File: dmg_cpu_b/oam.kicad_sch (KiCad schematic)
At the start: 130 parts

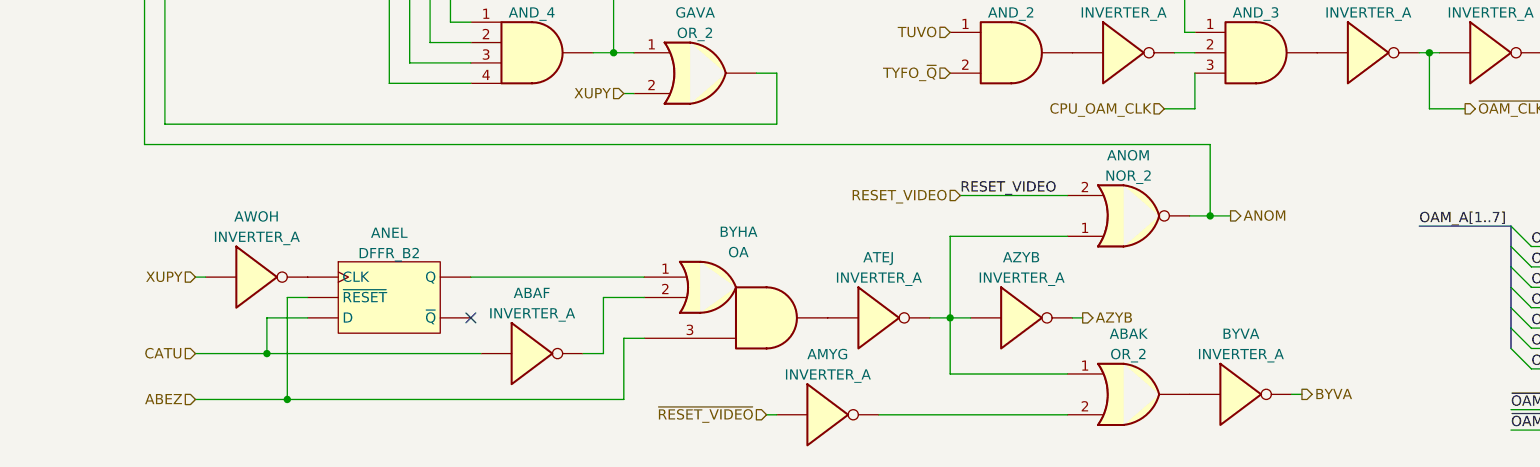
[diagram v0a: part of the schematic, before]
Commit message: sprite y comparator added
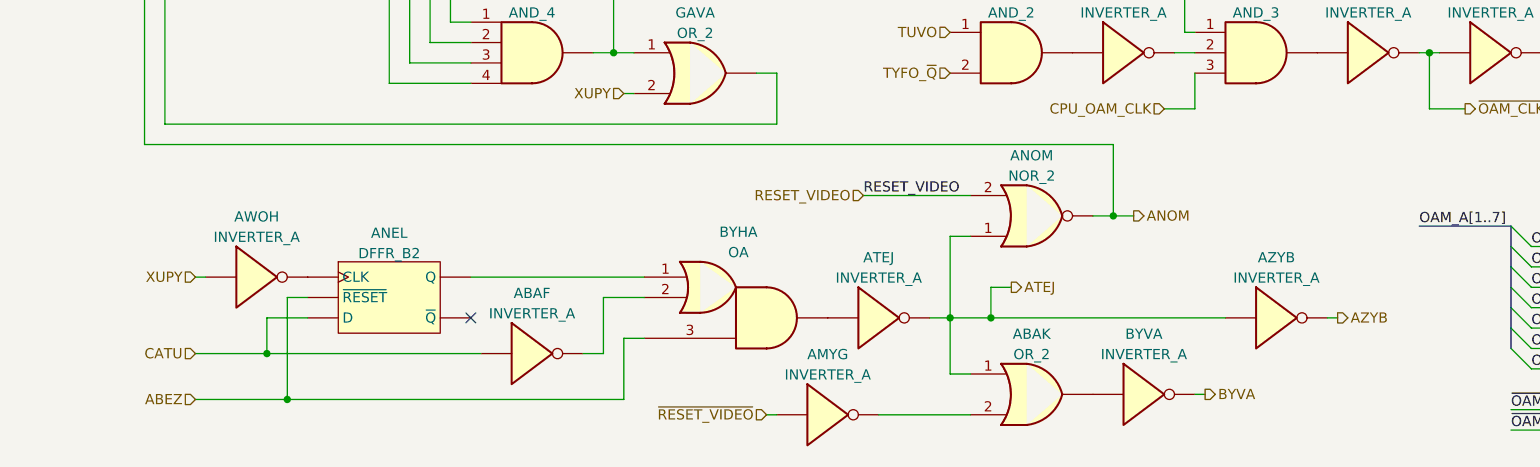
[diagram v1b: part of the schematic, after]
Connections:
- net ATEJ: now reaches ABAK.1, ANOM.1, ATEJ.2, AZYB.1
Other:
- moved on the sheet: ABAK, ANOM, AZYB, BYVA
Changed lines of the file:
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@@
   (junction (at 50.8 196.85) (diameter 0) (color 0 0 0 0)
   )
+  (junction (at 120.65 267.97) (diameter 0) (color 0 0 0 0)
+  )
   (junction (at 15.24 179.705) (diameter 0) (color 0 0 0 0)
   )
@@
   (junction (at 70.485 24.13) (diameter 0) (color 0 0 0 0)
   )
-  (junction (at 147.955 255.27) (diameter 0) (color 0 0 0 0)
+  (junction (at 135.89 255.27) (diameter 0) (color 0 0 0 0)
   )
   (junction (at 197.485 50.8) (diameter 0) (color 0 0 0 0)
@@
     (stroke (width 0) (type default) (color 0 0 0 0))
   )
-  (wire (pts (xy 115.57 267.97) (xy 118.11 267.97))
+  (wire (pts (xy 115.57 267.97) (xy 120.65 267.97))
     (stroke (width 0) (type default) (color 0 0 0 0))
   )
@@
     (stroke (width 0) (type default) (color 0 0 0 0))
   )
-  (wire (pts (xy 130.81 267.97) (xy 132.08 267.97))
+  (wire (pts (xy 162.56 267.97) (xy 163.83 267.97))
     (stroke (width 0) (type default) (color 0 0 0 0))
   )
@@
     (stroke (width 0) (type default) (color 0 0 0 0))
   )
+  (wire (pts (xy 120.65 267.97) (xy 149.86 267.97))
+    (stroke (width 0) (type default) (color 0 0 0 0))
+  )
   (wire (pts (xy 241.935 171.45) (xy 241.935 186.055))
     (stroke (width 0) (type default) (color 0 0 0 0))
@@
     (stroke (width 0) (type default) (color 0 0 0 0))
   )
-  (wire (pts (xy 130.175 280.035) (xy 106.68 280.035))
+  (wire (pts (xy 118.11 280.035) (xy 106.68 280.035))
     (stroke (width 0) (type default) (color 0 0 0 0))
   )
@@
     (stroke (width 0) (type default) (color 0 0 0 0))
   )
-  (wire (pts (xy 116.84 252.73) (xy 130.175 252.73))
+  (wire (pts (xy 104.775 252.73) (xy 118.11 252.73))
     (stroke (width 0) (type default) (color 0 0 0 0))
   )
@@
     (stroke (width 0) (type default) (color 0 0 0 0))
   )
+  (wire (pts (xy 123.19 264.16) (xy 120.65 264.16))
+    (stroke (width 0) (type default) (color 0 0 0 0))
+  )
   (wire (pts (xy 373.38 156.845) (xy 373.38 171.45))
     (stroke (width 0) (type default) (color 0 0 0 0))
@@
     (stroke (width 0) (type default) (color 0 0 0 0))
   )
-  (wire (pts (xy 147.955 255.27) (xy 145.415 255.27))
+  (wire (pts (xy 135.89 255.27) (xy 133.35 255.27))
     (stroke (width 0) (type default) (color 0 0 0 0))
   )
@@
     (stroke (width 0) (type default) (color 0 0 0 0))
   )
-  (wire (pts (xy 158.115 277.495) (xy 159.385 277.495))
+  (wire (pts (xy 146.05 277.495) (xy 147.32 277.495))
     (stroke (width 0) (type default) (color 0 0 0 0))
   )
@@
     (stroke (width 0) (type default) (color 0 0 0 0))
   )
-  (wire (pts (xy 115.57 274.955) (xy 130.175 274.955))
+  (wire (pts (xy 115.57 274.955) (xy 118.11 274.955))
     (stroke (width 0) (type default) (color 0 0 0 0))
   )
@@
     (stroke (width 0) (type default) (color 0 0 0 0))
   )
-  (wire (pts (xy 147.955 246.38) (xy 147.955 255.27))
+  (wire (pts (xy 135.89 246.38) (xy 135.89 255.27))
     (stroke (width 0) (type default) (color 0 0 0 0))
   )
@@
     (stroke (width 0) (type default) (color 0 0 0 0))
   )
+  (wire (pts (xy 120.65 264.16) (xy 120.65 267.97))
+    (stroke (width 0) (type default) (color 0 0 0 0))
+  )
   (wire (pts (xy 344.805 133.985) (xy 358.14 133.985))
     (stroke (width 0) (type default) (color 0 0 0 0))
@@
     (stroke (width 0) (type default) (color 0 0 0 0))
   )
-  (wire (pts (xy 15.24 246.38) (xy 147.955 246.38))
+  (wire (pts (xy 15.24 246.38) (xy 135.89 246.38))
     (stroke (width 0) (type default) (color 0 0 0 0))
   )
@@
     (stroke (width 0) (type default) (color 0 0 0 0))
   )
-  (wire (pts (xy 150.495 255.27) (xy 147.955 255.27))
+  (wire (pts (xy 138.43 255.27) (xy 135.89 255.27))
     (stroke (width 0) (type default) (color 0 0 0 0))
   )
@@
     (stroke (width 0) (type default) (color 0 0 0 0))
   )
-  (wire (pts (xy 130.175 257.81) (xy 115.57 257.81))
+  (wire (pts (xy 118.11 257.81) (xy 115.57 257.81))
     (stroke (width 0) (type default) (color 0 0 0 0))
   )
@@
     (effects (font (size 1.27 1.27)) (justify right bottom))
   )
-  (label "RESET_VIDEO" (at 116.84 252.73 0)
+  (label "RESET_VIDEO" (at 104.775 252.73 0)
     (effects (font (size 1.27 1.27)) (justify left bottom))
   )
@@
     (effects (font (size 1.27 1.27)) (justify left))
   )
-  (hierarchical_label "BYVA" (shape output) (at 159.385 277.495 0)
+  (hierarchical_label "BYVA" (shape output) (at 147.32 277.495 0)
     (effects (font (size 1.27 1.27)) (justify left))
   )
@@
     (effects (font (size 1.27 1.27)) (justify right))
   )
+  (hierarchical_label "ATEJ" (shape output) (at 123.19 264.16 0)
+    (effects (font (size 1.27 1.27)) (justify left))
+  )
   (hierarchical_label "AVAP" (shape input) (at 86.36 209.55 180)
     (effects (font (size 1.27 1.27)) (justify right))
   )
-  (hierarchical_label "AZYB" (shape output) (at 132.08 267.97 0)
+  (hierarchical_label "AZYB" (shape output) (at 163.83 267.97 0)
     (effects (font (size 1.27 1.27)) (justify left))
   )
@@
     (effects (font (size 1.27 1.27)) (justify right))
   )
-  (hierarchical_label "ANOM" (shape output) (at 150.495 255.27 0)
+  (hierarchical_label "ANOM" (shape output) (at 138.43 255.27 0)
     (effects (font (size 1.27 1.27)) (justify left))
   )
@@
     (effects (font (size 1.27 1.27)) (justify right))
   )
-  (hierarchical_label "RESET_VIDEO" (shape input) (at 116.84 252.73 180)
+  (hierarchical_label "RESET_VIDEO" (shape input) (at 104.775 252.73 180)
     (effects (font (size 1.27 1.27)) (justify right))
   )
@@
     (pin "2")
   )
-  (symbol (lib_id "DMG_CPU_Cells:INVERTER_A") (at 151.765 277.495 0) (unit 1)
+  (symbol (lib_id "DMG_CPU_Cells:INVERTER_A") (at 139.7 277.495 0) (unit 1)
     (in_bom yes) (on_board yes) (fields_autoplaced)
-    (property "Reference" "BYVA" (id 0) (at 151.765 269.9852 0))
-    (property "Value" "INVERTER_A" (id 1) (at 151.765 272.5221 0))
-    (property "Footprint" "" (id 2) (at 149.225 277.495 0)
+    (property "Reference" "BYVA" (id 0) (at 139.7 269.9852 0))
+    (property "Value" "INVERTER_A" (id 1) (at 139.7 272.5221 0))
+    (property "Footprint" "" (id 2) (at 137.16 277.495 0)
       (effects (font (size 1.27 1.27)) hide)
     )
-    (property "Datasheet" "http://iceboy.a-singer.de/doc/dmg_cells.html#inv_a" (id 3) (at 153.035 285.115 0)
+    (property "Datasheet" "http://iceboy.a-singer.de/doc/dmg_cells.html#inv_a" (id 3) (at 140.97 285.115 0)
       (effects (font (size 1.27 1.27)) hide)
     )
@@
     (pin "2")
   )
-  (symbol (lib_id "DMG_CPU_Cells:OR_2") (at 137.795 277.495 0) (unit 1)
+  (symbol (lib_id "DMG_CPU_Cells:OR_2") (at 125.73 277.495 0) (unit 1)
     (in_bom yes) (on_board yes) (fields_autoplaced)
-    (property "Reference" "ABAK" (id 0) (at 137.7948 269.9852 0))
-    (property "Value" "OR_2" (id 1) (at 137.7948 272.5221 0))
-    (property "Footprint" "" (id 2) (at 137.541 277.495 0)
+    (property "Reference" "ABAK" (id 0) (at 125.7298 269.9852 0))
+    (property "Value" "OR_2" (id 1) (at 125.7298 272.5221 0))
+    (property "Footprint" "" (id 2) (at 125.476 277.495 0)
       (effects (font (size 1.27 1.27)) hide)
     )
-    (property "Datasheet" "http://iceboy.a-singer.de/doc/dmg_cells.html#or2" (id 3) (at 137.795 285.115 0)
+    (property "Datasheet" "http://iceboy.a-singer.de/doc/dmg_cells.html#or2" (id 3) (at 125.73 285.115 0)
       (effects (font (size 1.27 1.27)) hide)
     )
@@
     (pin "1")
   )
-  (symbol (lib_id "DMG_CPU_Cells:NOR_2") (at 137.795 255.27 0) (mirror x) (unit 1)
+  (symbol (lib_id "DMG_CPU_Cells:NOR_2") (at 125.73 255.27 0) (mirror x) (unit 1)
     (in_bom yes) (on_board yes) (fields_autoplaced)
-    (property "Reference" "ANOM" (id 0) (at 137.7948 247.7602 0))
-    (property "Value" "NOR_2" (id 1) (at 137.7948 250.2971 0))
-    (property "Footprint" "" (id 2) (at 137.541 255.27 0)
+    (property "Reference" "ANOM" (id 0) (at 125.7298 247.7602 0))
+    (property "Value" "NOR_2" (id 1) (at 125.7298 250.2971 0))
+    (property "Footprint" "" (id 2) (at 125.476 255.27 0)
       (effects (font (size 1.27 1.27)) hide)
     )
-    (property "Datasheet" "http://iceboy.a-singer.de/doc/dmg_cells.html#nor2" (id 3) (at 137.795 247.65 0)
+    (property "Datasheet" "http://iceboy.a-singer.de/doc/dmg_cells.html#nor2" (id 3) (at 125.73 247.65 0)
       (effects (font (size 1.27 1.27)) hide)
     )
@@
     (pin "3")
   )
-  (symbol (lib_id "DMG_CPU_Cells:INVERTER_A") (at 124.46 267.97 0) (unit 1)
+  (symbol (lib_id "DMG_CPU_Cells:INVERTER_A") (at 156.21 267.97 0) (unit 1)
     (in_bom yes) (on_board yes) (fields_autoplaced)
-    (property "Reference" "AZYB" (id 0) (at 124.46 260.4602 0))
-    (property "Value" "INVERTER_A" (id 1) (at 124.46 262.9971 0))
-    (property "Footprint" "" (id 2) (at 121.92 267.97 0)
+    (property "Reference" "AZYB" (id 0) (at 156.21 260.4602 0))
+    (property "Value" "INVERTER_A" (id 1) (at 156.21 262.9971 0))
+    (property "Footprint" "" (id 2) (at 153.67 267.97 0)
       (effects (font (size 1.27 1.27)) hide)
     )
-    (property "Datasheet" "http://iceboy.a-singer.de/doc/dmg_cells.html#inv_a" (id 3) (at 125.73 275.59 0)
+    (property "Datasheet" "http://iceboy.a-singer.de/doc/dmg_cells.html#inv_a" (id 3) (at 157.48 275.59 0)
       (effects (font (size 1.27 1.27)) hide)
     )

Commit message: more oam sheets added. Some are still work in progress.
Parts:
- removed ABAF, AMYG, ATEJ, AWOH, AZYB, BYVA, XUJA: INVERTER_A, symbol DMG_CPU_Cells:INVERTER_A
- removed ABAK, ASEN, GAVA: OR_2, symbol DMG_CPU_Cells:OR_2
- removed ANEL, ELYN, FAHA, FONY, GOSO, WEWY, YFEL: DFFR_B2, symbol DMG_CPU_Cells:DFFR_B2
- removed ANOM: NOR_2, symbol DMG_CPU_Cells:NOR_2
- removed BESU: NOR_LATCH, symbol DMG_CPU_Cells:NOR_LATCH
- removed BYHA: OA, symbol DMG_CPU_Cells:OA
- removed FETO: AND_4, symbol DMG_CPU_Cells:AND_4
- removed WEFY: AND_2, symbol DMG_CPU_Cells:AND_2
- added CYKE, WUDA: INVERTER_B, symbol DMG_CPU_Cells:INVERTER_B
- added WEZA, WUCO, WUZY, WYDA, WYSE, ZYSU: TRI_INV_IF0, symbol DMG_CPU_Cells:TRI_INV_IF0
- added XADU, XECU, XEDY, XOBE, YDUF, ZUZE: DFFR_B, symbol DMG_CPU_Cells:DFFR_B
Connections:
- net +5V: now also XADU.1 (~{RESET}), XADU.5 (~{RESET}), XECU.1 (~{RESET}), XECU.5 (~{RESET}), XEDY.1 (~{RESET}), XEDY.5 (~{RESET}), XOBE.1 (~{RESET}), XOBE.5 (~{RESET}), YDUF.1 (~{RESET}), YDUF.5 (~{RESET}), ZUZE.1 (~{RESET}), ZUZE.5 (~{RESET})
- net AMAB: now also AMAB.3, APAG.2
- net OAM_A2: now also XADU.2 (D)
- net OAM_A3: now also XEDY.2 (D)
- net OAM_A4: now also ZUZE.2 (D)
- net OAM_A5: now also XOBE.2 (D)
- net OAM_A6: now also YDUF.2 (D)
- net OAM_A7: now also XECU.2 (D)
- net OAM_RENDER_A2: now also WUZY.3
- net OAM_RENDER_A3: now also WYSE.3
- net OAM_RENDER_A4: now also ZYSU.3
- net OAM_RENDER_A5: now also WYDA.3
- net OAM_RENDER_A6: now also WUCO.3
- net OAM_RENDER_A7: now also WEZA.3
- net XUPY: now also CYKE.1
- net XUJA: now reaches ASYT.2
- net BESU renamed OAM_PARSING
- new net: WYSE.2, XEDY.6 (~{Q})
- new net: WUDA.2, XADU.3 (CLK), XADU.4 (~{CLK}), XECU.3 (CLK), XECU.4 (~{CLK}), XEDY.3 (CLK), XEDY.4 (~{CLK}), XOBE.3 (CLK), XOBE.4 (~{CLK}), YDUF.3 (CLK), YDUF.4 (~{CLK}), ZUZE.3 (CLK), ZUZE.4 (~{CLK})
- new net: WUCO.2, YDUF.6 (~{Q})
- new net: WUZY.2, XADU.6 (~{Q})
- new net: WEZA.2, XECU.6 (~{Q})
- new net: ZUZE.6 (~{Q}), ZYSU.2
- new net: WYDA.2, XOBE.6 (~{Q})
- new net: CYKE.2, WUDA.1
- new net OAM_RENDERING: WEZA.1 (~{ENA}), WUCO.1 (~{ENA}), WUZY.1 (~{ENA}), WYDA.1 (~{ENA}), WYSE.1 (~{ENA}), ZYSU.1 (~{ENA})
- no-connect marks 4 -> 8
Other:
- moved on the sheet: ACYL, AJEP, AJON, AJUJ, AMAB, APAR, ASAM, ASYT, BETE, BODE, BOGE, MAKA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

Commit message: More OAM sheets added.
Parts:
- added AVER: NAND_2, symbol DMG_CPU_Cells:NAND_2
- added BYCU: NAND_3, symbol DMG_CPU_Cells:NAND_3
- added COTA: INVERTER_B, symbol DMG_CPU_Cells:INVERTER_B
- added CUFE: OAI, symbol DMG_CPU_Cells:OAI
- added VAPE: AND_2, symbol DMG_CPU_Cells:AND_2
- added XUJY: INVERTER_A, symbol DMG_CPU_Cells:INVERTER_A
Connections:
- net DMA_RUN: now also CUFE.2
- net FEXX: now also CUFE.1
- net ~{DMA_PHI}: now also NAXY.1; no longer NAXY.2
- net at MAKA.6 (Q): now also NAXY.2; no longer NAXY.1
- net OAM_ADDR_PARSE renamed MODE1
- net MODE1: now also AVER.1
- net XOCE_1MHz renamed XOCE
- new net: BYCU.1, CUFE.4
- new net: BYCU.2, XUJY.2
- new net: AVER.3, BYCU.3
- new net: BYCU.4, COTA.1
- new net: VAPE.3, XUJY.1
- new net COTA: COTA.2
- new net DMA_PHI: CUFE.3
- new net TACU: VAPE.1
- new net TUVO: VAPE.2
- new net XYSO: AVER.2
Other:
- moved on the sheet: AJEP, ASYT, BODE, CYKE, MAKA, NAXY, OAM_A, OAM_B, POWU, WEZA, WUCO, WUDA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

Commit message: All sheets captured. Serious tidying is required in PPU section.
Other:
- company: (none) -> CC-BY-SA-4.0 Régis Galland & Michael Singer -- Derived work from Furrtek
- title: (none) -> DMG CPU B
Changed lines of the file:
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@@
 (kicad_sch (version 20211123) (generator eeschema)
   (paper "A3")
+  (title_block
+    (title "DMG CPU B")
+    (date "2022-05-19")
+    (rev "0")
+    (company "CC-BY-SA-4.0 Régis Galland & Michael Singer -- Derived work from Furrtek")
+    (comment 1 "https://github.com/msinger/dmg-schematics")
+  )
   (junction (at 78.105 88.9) (diameter 0) (color 0 0 0 0)
   )

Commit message: Changes made based on review. PPU hierarchcal sheet work started.
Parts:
- added BOFE, CATY, DECY: INVERTER_A, symbol DMG_CPU_Cells:INVERTER_A
- added BOTA: NAND_3, symbol DMG_CPU_Cells:NAND_3
- added LEKO: INVERTER_B, symbol DMG_CPU_Cells:INVERTER_B
- added MYNU: NAND_2, symbol DMG_CPU_Cells:NAND_2
- ASAM: value NOR_3 -> OR_3; symbol DMG_CPU_Cells:NOR_3 -> DMG_CPU_Cells:OR_3
- renumbered WUVE to WUWE
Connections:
- net +5V: now also GECA.2, WYDU.2; no longer GEFY.2, WUWE.2
- net FEXX: now also BOTA.2
- net GND: now also GEFY.2, WUWE.2; no longer GECA.2, WYDU.2
- net ~{OAM_A_RD}: no longer OAM_A.8 (~{OE})
- net ~{OAM_B_RD}: no longer OAM_B.8 (~{OE})
- net OAM_RAM_CHIP_SEL: now reaches FODO.3, GARO.3, GECA.3, GEFY.3, GEKA.1
- net AMAB: no longer names the net of AMAB.3, APAG.2, GUKO.2, WUKU.2, WYJA.1
- net CPU_OAM_CLK renamed CPU_OAM_RD
- net CPU_OAM_RD: now also BOTA.4
- net OAM_CLK renamed ~{OAM_CS}
- net ~{OAM_CS}: now also OAM_A.8 (~{OE}), OAM_B.8 (~{OE})
- net OAM_PHI: no longer names the net of MAKA.3 (D)
- net OAM_PHI: now also BOFE.1, CATY.2, MYNU.2
- net OAM_RD: no longer names the net of GUKO.3, WUKU.1
- net OAM_RD: now also LEKO.2
- net OAM_WR: no longer names the net of WYJA.4, YLYC.1, YNYC.2
- net ~{OAM_CLK} renamed OAM_DATA_LATCH
- new net: LEKO.1, MYNU.3
- new net: BOFE.2, BOTA.1
- new net: CATY.1, DECY.2
- new net CPU_PHI2: DECY.1
- new net PPU_RD: BOTA.3, MYNU.1
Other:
- note added: "OAM data is permanently latched outside of CPU RD cycle"
- moved on the sheet: ACOT, ACYL, ADAH, AGYK, AJEP, AJON, AJUJ, AMAB, AMUH, ANUM, APAG, APAR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

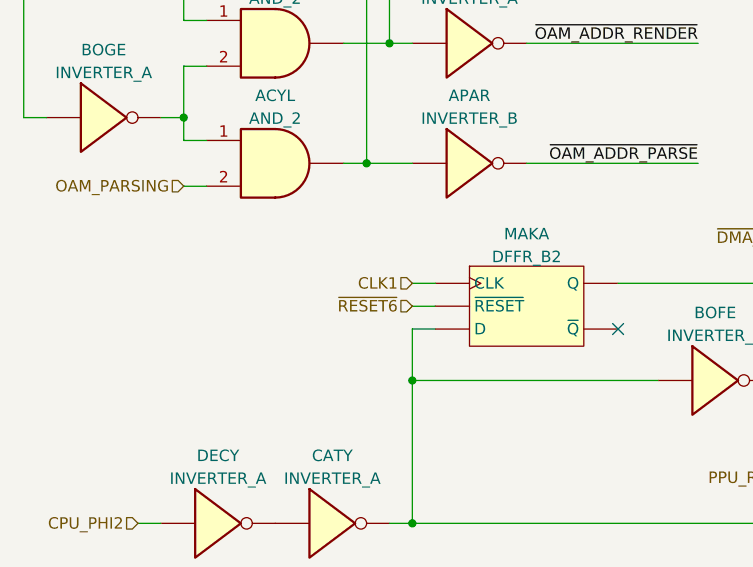
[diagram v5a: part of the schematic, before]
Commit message: PPU hierarchical page progress. Elements moved out of window sheet to be includes in BG and WIN cycles sheet
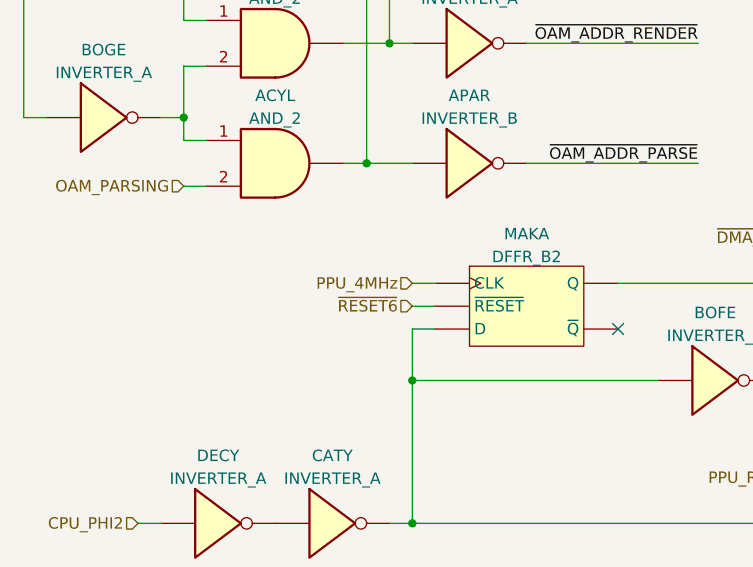
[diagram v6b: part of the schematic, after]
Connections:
- net CLK1 renamed PPU_4MHz
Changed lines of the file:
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@@
     (effects (font (size 1.27 1.27)) (justify right))
   )
-  (hierarchical_label "CLK1" (shape input) (at 57.785 104.775 180)
+  (hierarchical_label "PPU_4MHz" (shape input) (at 57.785 104.775 180)
     (effects (font (size 1.27 1.27)) (justify right))
   )
